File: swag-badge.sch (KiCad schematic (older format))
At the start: 10 parts, among them J1 OLED_1, J2 OLED_2, J3 Lolin32, J4 SAO_3, J5 SAO_1, J6 SAO_2, J7 Touch_slider_01, J8 Touch_slider_02, SW1 SW_Push, SW2 SW_Push

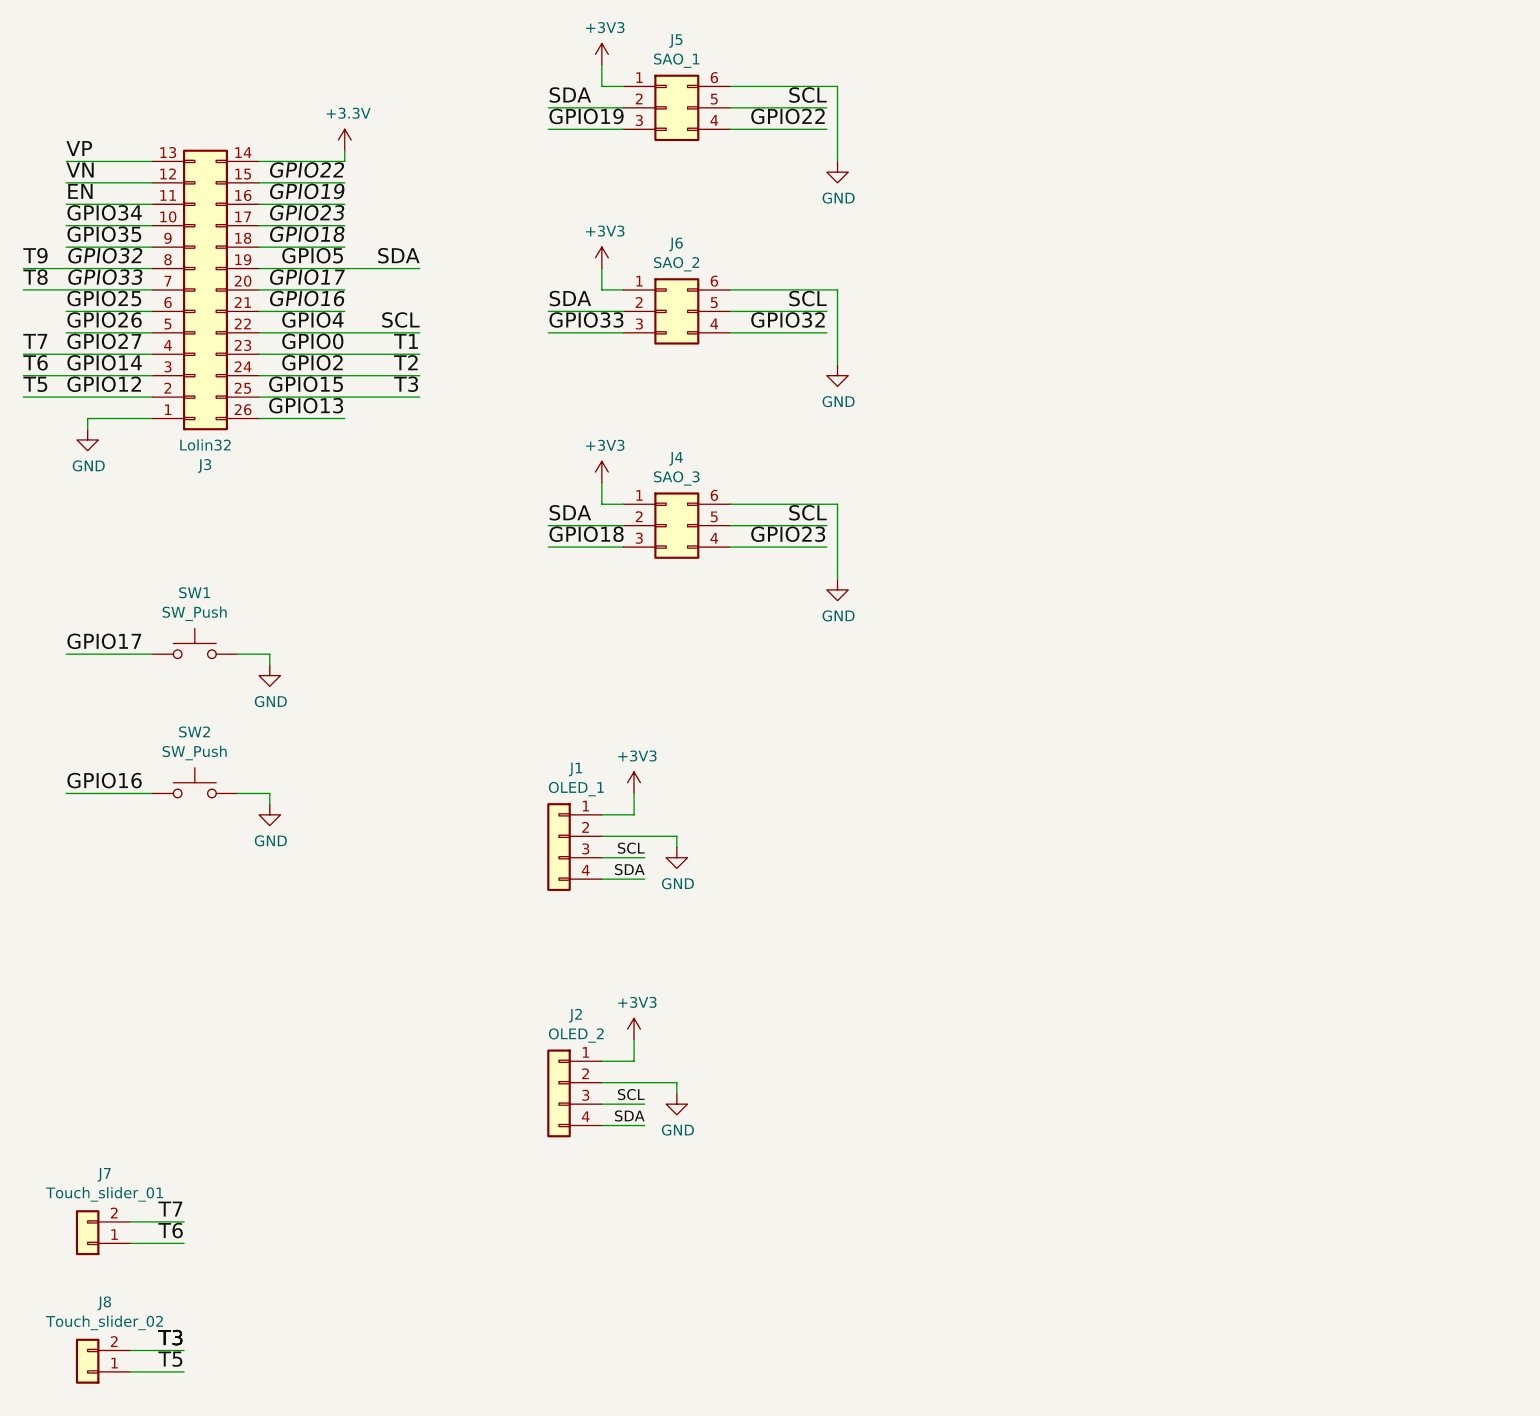
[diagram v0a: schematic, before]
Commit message: 4th SAO added
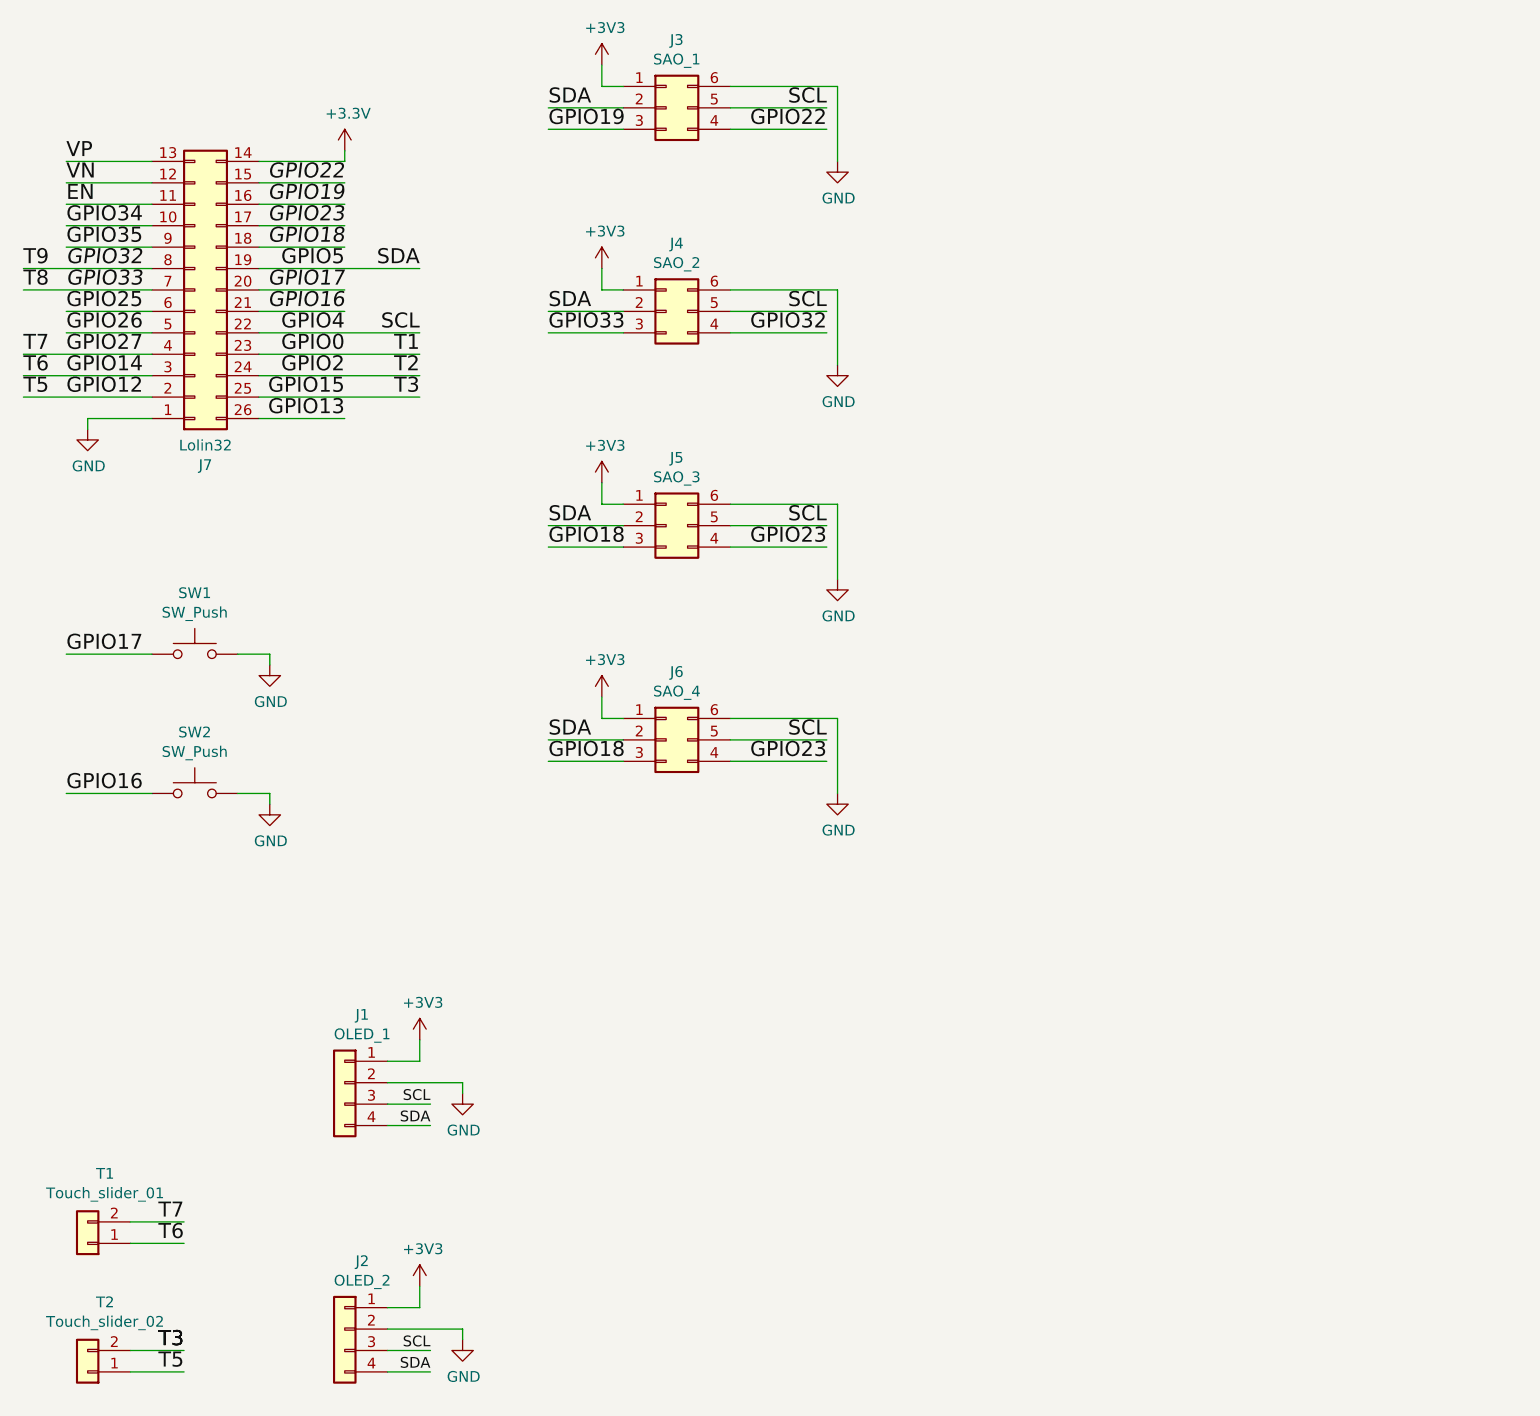
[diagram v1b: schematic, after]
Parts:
- added J6: SAO_4, SwagBadge:SAO_Header_6-Pin, symbol Connector_Generic:Conn_02x03_Counter_Clockwise
- renumbered J5 to J3, J6 to J4, J4 to J5, J3 to J7, J7 to T1, J8 to T2
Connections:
- net +3V3: now also J6.1 (Pin_1)
- net GND: now also J6.6 (Pin_6)
- net GPIO18: now also J6.3 (Pin_3)
- net GPIO23: now also J6.4 (Pin_4)
- net GPIO4: now also J6.5 (Pin_5)
- net GPIO5: now also J6.2 (Pin_2)
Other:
- moved on the sheet: J1, J2
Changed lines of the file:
@@
 L Connector_Generic:Conn_01x04 J1
 U 1 1 5F5375FF
-P 3500 4550
-F 0 "J1" H 3418 4867 50  0000 C CNN
-F 1 "OLED_1" H 3418 4776 50  0000 C CNN
-F 2 "SwagBadge:Display_Module_128X64_I2C_SSD1306" H 3500 4550 50  0001 C CNN
-F 3 "~" H 3500 4550 50  0001 C CNN
-	1    3500 4550
+P 2500 5700
+F 0 "J1" H 2418 6017 50  0000 C CNN
+F 1 "OLED_1" H 2418 5926 50  0000 C CNN
+F 2 "SwagBadge:Display_Module_128X64_I2C_SSD1306" H 2500 5700 50  0001 C CNN
+F 3 "~" H 2500 5700 50  0001 C CNN
+	1    2500 5700
 	-1   0    0    -1
 $EndComp
@@
 L Connector_Generic:Conn_01x04 J2
 U 1 1 5F53A38D
-P 3500 5700
-F 0 "J2" H 3418 6017 50  0000 C CNN
-F 1 "OLED_2" H 3418 5926 50  0000 C CNN
-F 2 "SwagBadge:Display_Module_128X64_I2C_SSD1306" H 3500 5700 50  0001 C CNN
-F 3 "~" H 3500 5700 50  0001 C CNN
-	1    3500 5700
+P 2500 6850
+F 0 "J2" H 2418 7167 50  0000 C CNN
+F 1 "OLED_2" H 2418 7076 50  0000 C CNN
+F 2 "SwagBadge:Display_Module_128X64_I2C_SSD1306" H 2500 6850 50  0001 C CNN
+F 3 "~" H 2500 6850 50  0001 C CNN
+	1    2500 6850
 	-1   0    0    -1
 $EndComp
 $Comp
-L Connector_Generic:Conn_02x03_Counter_Clockwise J5
+L Connector_Generic:Conn_02x03_Counter_Clockwise J3
 U 1 1 5F53AD7D
 P 4000 1150
-F 0 "J5" H 4050 1467 50  0000 C CNN
+F 0 "J3" H 4050 1467 50  0000 C CNN
 F 1 "SAO_1" H 4050 1376 50  0000 C CNN
 F 2 "SwagBadge:SAO_Header_6-Pin" H 4000 1150 50  0001 C CNN
@@
 L power:+3V3 #PWR0106
 U 1 1 5F53F1EB
-P 3850 4350
-F 0 "#PWR0106" H 3850 4200 50  0001 C CNN
-F 1 "+3V3" H 3865 4523 50  0000 C CNN
-F 2 "" H 3850 4350 50  0001 C CNN
-F 3 "" H 3850 4350 50  0001 C CNN
-	1    3850 4350
-	1    0    0    -1
-$EndComp
-Text Label 3900 4750 2    50   ~ 0
-SDA
-Text Label 3900 4650 2    50   ~ 0
-SCL
-Wire Wire Line
-	3700 4650 3900 4650
-Wire Wire Line
-	3700 4750 3900 4750
-Wire Wire Line
-	3700 4450 3850 4450
-Wire Wire Line
-	3850 4450 3850 4350
+P 2850 5500
+F 0 "#PWR0106" H 2850 5350 50  0001 C CNN
+F 1 "+3V3" H 2865 5673 50  0000 C CNN
+F 2 "" H 2850 5500 50  0001 C CNN
+F 3 "" H 2850 5500 50  0001 C CNN
+	1    2850 5500
+	1    0    0    -1
+$EndComp
+Text Label 2900 5900 2    50   ~ 0
+SDA
+Text Label 2900 5800 2    50   ~ 0
+SCL
+Wire Wire Line
+	2700 5800 2900 5800
+Wire Wire Line
+	2700 5900 2900 5900
+Wire Wire Line
+	2700 5600 2850 5600
+Wire Wire Line
+	2850 5600 2850 5500
 $Comp
 L power:GND #PWR0107
 U 1 1 5F5403D5
-P 4050 4600
-F 0 "#PWR0107" H 4050 4350 50  0001 C CNN
-F 1 "GND" H 4055 4427 50  0000 C CNN
-F 2 "" H 4050 4600 50  0001 C CNN
-F 3 "" H 4050 4600 50  0001 C CNN
-	1    4050 4600
-	1    0    0    -1
-$EndComp
-Wire Wire Line
-	3700 4550 4050 4550
-Wire Wire Line
-	4050 4550 4050 4600
+P 3050 5750
+F 0 "#PWR0107" H 3050 5500 50  0001 C CNN
+F 1 "GND" H 3055 5577 50  0000 C CNN
+F 2 "" H 3050 5750 50  0001 C CNN
+F 3 "" H 3050 5750 50  0001 C CNN
+	1    3050 5750
+	1    0    0    -1
+$EndComp
+Wire Wire Line
+	2700 5700 3050 5700
+Wire Wire Line
+	3050 5700 3050 5750
 $Comp
 L power:+3V3 #PWR0108
 U 1 1 5F540D5F
-P 3850 5500
-F 0 "#PWR0108" H 3850 5350 50  0001 C CNN
-F 1 "+3V3" H 3865 5673 50  0000 C CNN
-F 2 "" H 3850 5500 50  0001 C CNN
-F 3 "" H 3850 5500 50  0001 C CNN
-	1    3850 5500
-	1    0    0    -1
-$EndComp
-Text Label 3900 5900 2    50   ~ 0
-SDA
-Text Label 3900 5800 2    50   ~ 0
-SCL
-Wire Wire Line
-	3700 5800 3900 5800
-Wire Wire Line
-	3700 5900 3900 5900
-Wire Wire Line
-	3700 5600 3850 5600
-Wire Wire Line
-	3850 5600 3850 5500
+P 2850 6650
+F 0 "#PWR0108" H 2850 6500 50  0001 C CNN
+F 1 "+3V3" H 2865 6823 50  0000 C CNN
+F 2 "" H 2850 6650 50  0001 C CNN
+F 3 "" H 2850 6650 50  0001 C CNN
+	1    2850 6650
+	1    0    0    -1
+$EndComp
+Text Label 2900 7050 2    50   ~ 0
+SDA
+Text Label 2900 6950 2    50   ~ 0
+SCL
+Wire Wire Line
+	2700 6950 2900 6950
+Wire Wire Line
+	2700 7050 2900 7050
+Wire Wire Line
+	2700 6750 2850 6750
+Wire Wire Line
+	2850 6750 2850 6650
 $Comp
 L power:GND #PWR0109
 U 1 1 5F540D6F
-P 4050 5750
-F 0 "#PWR0109" H 4050 5500 50  0001 C CNN
-F 1 "GND" H 4055 5577 50  0000 C CNN
-F 2 "" H 4050 5750 50  0001 C CNN
-F 3 "" H 4050 5750 50  0001 C CNN
-	1    4050 5750
-	1    0    0    -1
-$EndComp
-Wire Wire Line
-	3700 5700 4050 5700
-Wire Wire Line
-	4050 5700 4050 5750
+P 3050 6900
+F 0 "#PWR0109" H 3050 6650 50  0001 C CNN
+F 1 "GND" H 3055 6727 50  0000 C CNN
+F 2 "" H 3050 6900 50  0001 C CNN
+F 3 "" H 3050 6900 50  0001 C CNN
+	1    3050 6900
+	1    0    0    -1
+$EndComp
+Wire Wire Line
+	2700 6850 3050 6850
+Wire Wire Line
+	3050 6850 3050 6900
 $Comp
 L power:+3V3 #PWR0110
@@
 GPIO15
 $Comp
-L Connector_Generic:Conn_02x03_Counter_Clockwise J6
+L Connector_Generic:Conn_02x03_Counter_Clockwise J4
 U 1 1 5F6BCBBA
 P 4000 2100
-F 0 "J6" H 4050 2417 50  0000 C CNN
+F 0 "J4" H 4050 2417 50  0000 C CNN
 F 1 "SAO_2" H 4050 2326 50  0000 C CNN
 F 2 "SwagBadge:SAO_Header_6-Pin" H 4000 2100 50  0001 C CNN
@@
 $EndComp
 $Comp
-L Connector_Generic:Conn_02x13_Counter_Clockwise J3
+L Connector_Generic:Conn_02x13_Counter_Clockwise J7
 U 1 1 5F73663E
 P 1800 2000
-F 0 "J3" H 1850 2817 50  0000 C CNN
+F 0 "J7" H 1850 2817 50  0000 C CNN
 F 1 "Lolin32" H 1850 2726 50  0000 C CNN
 F 2 "SwagBadge:LOLIN32_Flipped_SmallCut" H 1800 2000 50  0001 C CNN
@@
 	2100 1500 2500 1500
 $Comp
-L Connector_Generic:Conn_02x03_Counter_Clockwise J4
+L Connector_Generic:Conn_02x03_Counter_Clockwise J5
 U 1 1 5F7685A3
 P 4000 3100
-F 0 "J4" H 4050 3417 50  0000 C CNN
+F 0 "J5" H 4050 3417 50  0000 C CNN
 F 1 "SAO_3" H 4050 3326 50  0000 C CNN
 F 2 "SwagBadge:SAO_Header_6-Pin" H 4000 3100 50  0001 C CNN
@@
 	1500 7050 1750 7050
 $Comp
-L Connector_Generic:Conn_01x02 J7
+L Connector_Generic:Conn_01x02 T1
 U 1 1 5F7E3B54
 P 1300 6450
-F 0 "J7" H 1218 6125 50  0000 C CNN
+F 0 "T1" H 1218 6125 50  0000 C CNN
 F 1 "Touch_slider_01" H 1218 6216 50  0000 C CNN
 F 2 "SwagBadge:Touch_Slider" H 1300 6450 50  0001 C CNN
@@
 $EndComp
 $Comp
-L Connector_Generic:Conn_01x02 J8
+L Connector_Generic:Conn_01x02 T2
 U 1 1 5F7E4758
 P 1300 7050
-F 0 "J8" H 1218 6725 50  0000 C CNN
+F 0 "T2" H 1218 6725 50  0000 C CNN
 F 1 "Touch_slider_02" H 1218 6816 50  0000 C CNN
 F 2 "SwagBadge:Touch_Slider" H 1300 7050 50  0001 C CNN
@@
 Wire Wire Line
 	1500 6950 1750 6950
+$Comp
+L Connector_Generic:Conn_02x03_Counter_Clockwise J6
+U 1 1 5F7D9ED3
+P 4000 4100
+F 0 "J6" H 4050 4417 50  0000 C CNN
+F 1 "SAO_4" H 4050 4326 50  0000 C CNN
+F 2 "SwagBadge:SAO_Header_6-Pin" H 4000 4100 50  0001 C CNN
+F 3 "~" H 4000 4100 50  0001 C CNN
+	1    4000 4100
+	1    0    0    -1
+$EndComp
+$Comp
+L power:GND #PWR0103
+U 1 1 5F7D9ED9
+P 4800 4350
+F 0 "#PWR0103" H 4800 4100 50  0001 C CNN
+F 1 "GND" H 4805 4177 50  0000 C CNN
+F 2 "" H 4800 4350 50  0001 C CNN
+F 3 "" H 4800 4350 50  0001 C CNN
+	1    4800 4350
+	1    0    0    -1
+$EndComp
+Wire Wire Line
+	3700 3900 3700 4000
+Wire Wire Line
+	3700 4000 3800 4000
+Wire Wire Line
+	4300 4000 4800 4000
+Wire Wire Line
+	4800 4000 4800 4350
+Wire Wire Line
+	3800 4100 3450 4100
+Wire Wire Line
+	3800 4200 3450 4200
+Wire Wire Line
+	4300 4100 4750 4100
+Wire Wire Line
+	4300 4200 4750 4200
+$Comp
+L power:+3V3 #PWR0113
+U 1 1 5F7D9EE7
+P 3700 3900
+F 0 "#PWR0113" H 3700 3750 50  0001 C CNN
+F 1 "+3V3" H 3715 4073 50  0000 C CNN
+F 2 "" H 3700 3900 50  0001 C CNN
+F 3 "" H 3700 3900 50  0001 C CNN
+	1    3700 3900
+	1    0    0    -1
+$EndComp
+Text Label 4750 4100 2    70   ~ 0
+SCL
+Text Label 3450 4100 0    70   ~ 0
+SDA
+Text Label 4750 4200 2    70   ~ 0
+GPIO23
+Text Label 3450 4200 0    70   ~ 0
+GPIO18
 $EndSCHEMATC

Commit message: Just SAO things.
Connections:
- net GPIO18: no longer J6.3 (Pin_3)
- net GPIO23: no longer J6.4 (Pin_4)
- new net GPIOXX: J6.3 (Pin_3), J6.4 (Pin_4)
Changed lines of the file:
@@
 SDA
 Text Label 4750 4200 2    70   ~ 0
-GPIO23
+GPIOXX
 Text Label 3450 4200 0    70   ~ 0
-GPIO18
+GPIOXX
 $EndSCHEMATC
